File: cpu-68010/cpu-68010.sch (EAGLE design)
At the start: 5 parts, among them X1 FABC96R

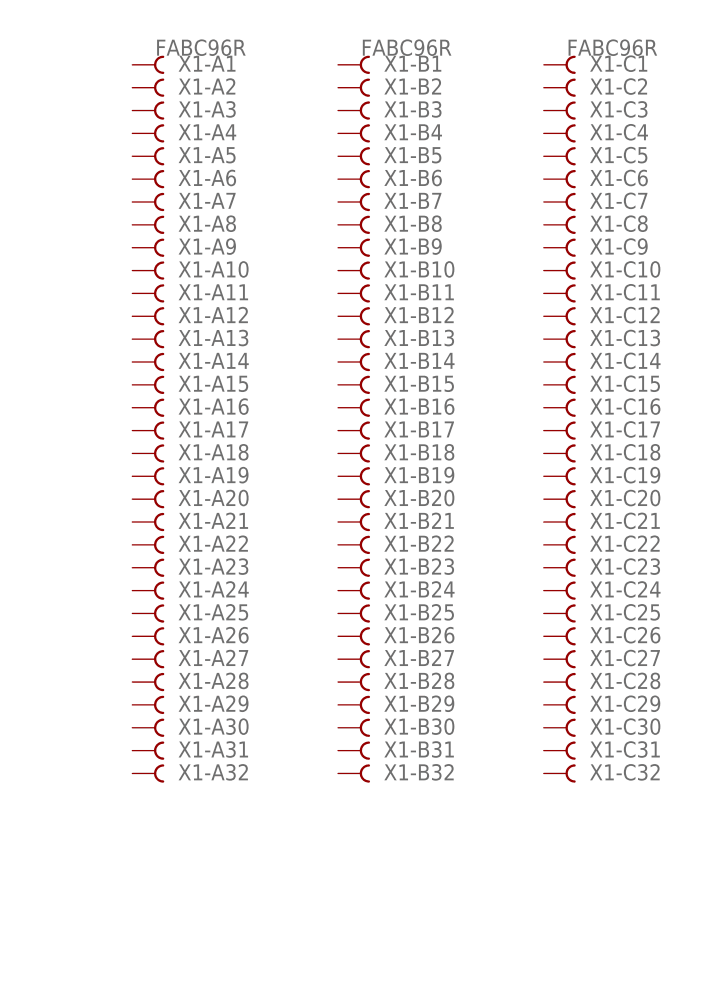
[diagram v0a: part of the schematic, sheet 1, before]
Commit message: added bus pinout description, basic connections for bus
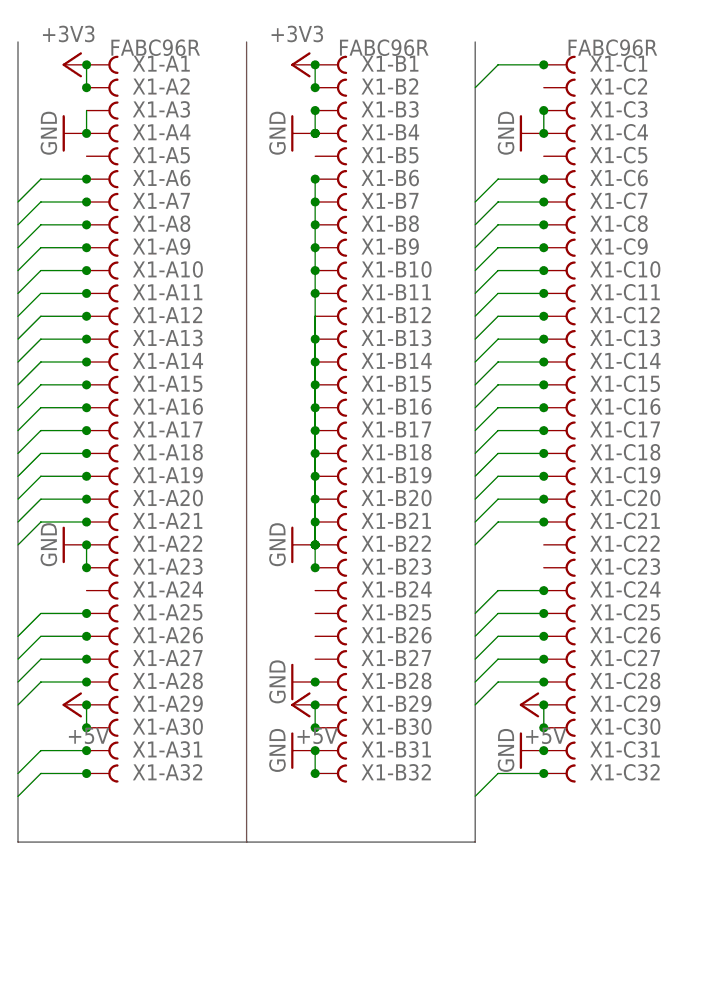
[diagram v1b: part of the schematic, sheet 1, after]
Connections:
- new net !BUS_ACK: X1-A28.B
- new net !BUS_IRQ: X1-A31.B
- new net !BUS_IRQACK: X1-A32.B
- new net !BUS_RESET: X1-C1.B
- new net !BUS_START: X1-C28.B
- new net +3V3: X1-A1.B, X1-A2.B, X1-B1.B, X1-B2.B
- new net BUS_AD0: X1-C6.B
- new net BUS_AD1: X1-A6.B
- new net BUS_AD10: X1-C11.B
- new net BUS_AD11: X1-A11.B
- new net BUS_AD12: X1-C12.B
- new net BUS_AD13: X1-A12.B
- new net BUS_AD14: X1-C13.B
- new net BUS_AD15: X1-A13.B
- new net BUS_AD16: X1-C14.B
- new net BUS_AD17: X1-A14.B
- new net BUS_AD18: X1-C15.B
- new net BUS_AD19: X1-A15.B
- new net BUS_AD2: X1-C7.B
- new net BUS_AD20: X1-C16.B
- new net BUS_AD21: X1-A16.B
- new net BUS_AD22: X1-C17.B
- new net BUS_AD23: X1-A17.B
- new net BUS_AD24: X1-C18.B
- new net BUS_AD25: X1-A18.B
- new net BUS_AD26: X1-C19.B
- new net BUS_AD27: X1-A19.B
- new net BUS_AD28: X1-C20.B
- new net BUS_AD29: X1-A20.B
- new net BUS_AD3: X1-A7.B
- new net BUS_AD30: X1-C21.B
- new net BUS_AD31: X1-A21.B
- new net BUS_AD4: X1-C8.B
- new net BUS_AD5: X1-A8.B
- new net BUS_AD6: X1-C9.B
- new net BUS_AD7: X1-A9.B
- new net BUS_AD8: X1-C10.B
- new net BUS_AD9: X1-A10.B
- new net BUS_CLK: X1-C32.B
- new net BUS_CONFIG: X1-A25.B
- new net BUS_CS0: X1-C26.B
- new net BUS_CS1: X1-A26.B
- new net BUS_CS2: X1-C27.B
- new net BUS_CS3: X1-A27.B
- new net BUS_MODE0: X1-C24.B
- new net BUS_MODE1: X1-C25.B
- net +5V: now also X1-A29.B, X1-A30.B, X1-B29.B, X1-B30.B, X1-C29.B, X1-C30.B
- net GND: now also X1-A22.B, X1-A23.B, X1-A3.B, X1-A4.B, X1-B10.B, X1-B11.B, X1-B12.B, X1-B13.B, X1-B14.B, X1-B15.B, X1-B16.B, X1-B17.B, X1-B18.B, X1-B19.B, X1-B20.B, X1-B21.B, X1-B22.B, X1-B23.B, X1-B28.B, X1-B3.B, X1-B31.B, X1-B32.B, X1-B4.B, X1-B6.B, X1-B7.B, X1-B8.B, X1-B9.B, X1-C3.B, X1-C31.B, X1-C4.B
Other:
- moved on the sheet: X1-A1, X1-A10, X1-A11, X1-A12, X1-A13, X1-A14, X1-A15, X1-A16, X1-A17, X1-A18, X1-A19, X1-A2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

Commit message: added psram to 68010 board
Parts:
- added C2, C5: 100nF, rcl:C-EUC0805
- added C4: 47µF, rcl:CPOL-EUCT6032
- added IC2: (no value), 68komputer:IS66WV51216EBLLTSOP-44
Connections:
- new net !RAM_CS: IC2.!CS1
- new net !RAM_LB: IC2.!LB
- new net !RAM_OE: IC2.!OE
- new net !RAM_UB: IC2.!UB
- new net !RAM_WE: IC2.!WE
- new net A1: IC2.A0
- new net A10: IC2.A9
- new net A11: IC2.A10
- new net A12: IC2.A11
- new net A13: IC2.A12
- new net A14: IC2.A13
- new net A15: IC2.A14
- new net A16: IC2.A15
- new net A17: IC2.A16
- new net A18: IC2.A17
- new net A19: IC2.A18
- new net A2: IC2.A1
- new net A3: IC2.A2
- new net A4: IC2.A3
- new net A5: IC2.A4
- new net A6: IC2.A5
- new net A7: IC2.A6
- new net A8: IC2.A7
- new net A9: IC2.A8
- new net D0: IC2.D0
- new net D1: IC2.D1
- new net D10: IC2.D10
- new net D11: IC2.D11
- new net D12: IC2.D12
- new net D13: IC2.D13
- new net D14: IC2.D14
- new net D15: IC2.D15
- new net D2: IC2.D2
- new net D3: IC2.D3
- new net D4: IC2.D4
- new net D5: IC2.D5
- new net D6: IC2.D6
- new net D7: IC2.D7
- new net D8: IC2.D8
- new net D9: IC2.D9
- net +3V3: now also C2.1, C4.+, C5.1, IC2.VDD
- net GND: now also C2.2, C4.-, C5.2, IC2.GND

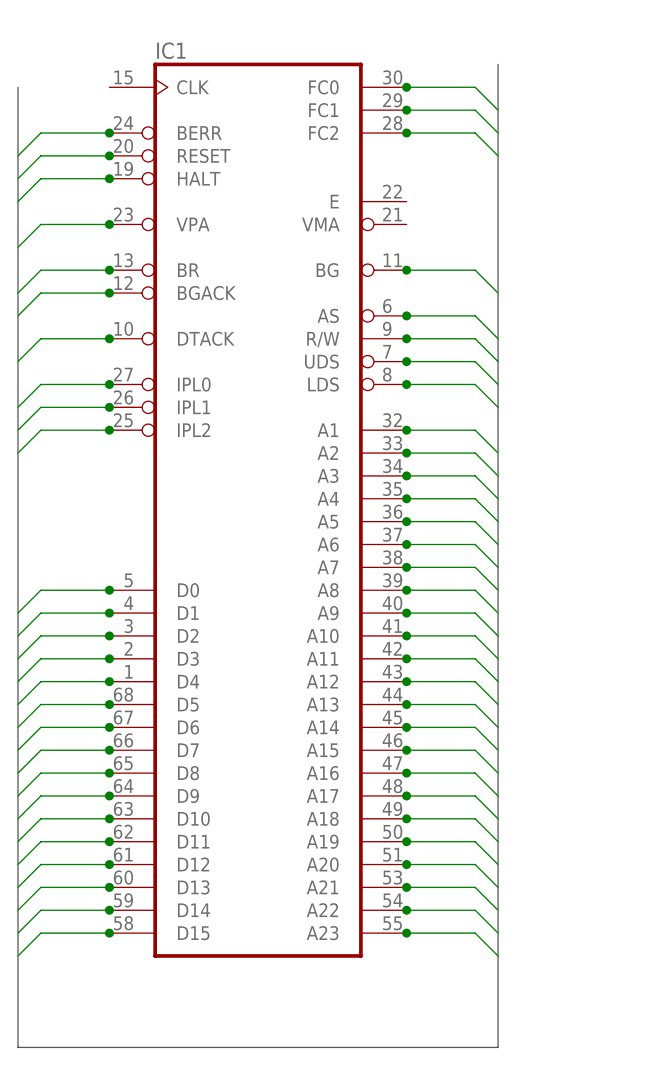
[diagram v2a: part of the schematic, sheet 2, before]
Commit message: cleaned up kerjigger somewhat
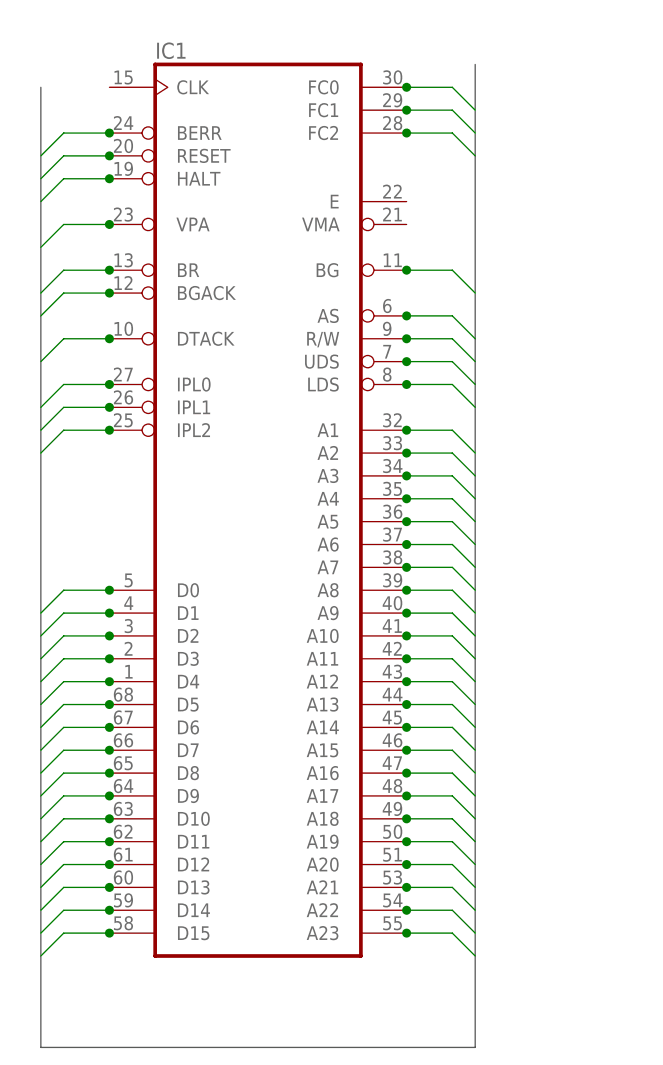
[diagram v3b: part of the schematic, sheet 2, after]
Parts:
- added C10, C12, C13, C7, C9: 100nF, rcl:C-EUC0805
- added C11, C8: 47µF, rcl:CPOL-EUCT6032
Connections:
- net +3V3: now also C10.1, C11.+, C12.1
- net +5V: now also C13.1, C7.1, C8.+, C9.1
- net GND: now also C10.2, C11.-, C12.2, C13.2, C7.2, C8.-, C9.2

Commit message: added address decoding, interrupt handling, external bus interface
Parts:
- added C14, C16, C17, C19, C20, C21, C23, C24, C25, C26: 100nF, rcl:C-EUC0805
- added C15, C18, C22: 47µF, rcl:CPOL-EUCT6032
- added C27, C28, C29, C30: 10µF, rcl:CPOL-EUE1.8-4
- added IC10, IC11: 74HC30D, 74xx-eu:74HC30D
- added IC12: 74HC85D, 74xx-eu:74HC85D
- added IC13: MAX232, maxim:MAX232
- added IC3, IC4: (no value), 68komputer:SST39SF0X0PDIP-32
- added IC5: (no value), 68komputer:DS1244EDIP-28
- added IC6: 74HC00D, 74xx-eu:74HC00D
- added IC7: 74HCT154DW, 74xx-eu:74HCT154DW
- added IC8: 74HC04D, 74xx-eu:74HC04D
- added IC9: 74HC148D, 74xx-eu:74HC148D
- added QG1: (no value), crystal:XO-8
- added R1: 10k, rcl:R-EU_R2012
- added X2: (no value), con-subd:F09HP
- C10: value 100nF -> 47µF; device rcl:C-EUC0805 -> rcl:CPOL-EUCT6032; MOUSER 710-885012207072 -> 581-TAJD476M016RNJV
- C11: value 47µF -> 100nF; device rcl:CPOL-EUCT6032 -> rcl:C-EUC0805; MOUSER 581-TAJD476M016RNJV -> 710-885012207072
- IC1: device micro-mc68000:MC68000FN-SOC -> 68komputer:MC68000FN-SOC
- IC2: device 68komputer:IS66WV51216EBLLTSOP-44 -> 68komputer:MC68901FN-SOC
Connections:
- removed net !68K_AS: IC1G$1.AS
- removed net !68K_BERR: IC1G$1.BERR
- removed net !68K_BG: IC1G$1.BG
- removed net !68K_BGACK: IC1G$1.BGACK
- removed net !68K_BR: IC1G$1.BR
- removed net !68K_DTACK: IC1G$1.DTACK
- removed net !68K_HALT: IC1G$1.HALT
- removed net !68K_IPL0: IC1G$1.IPL0
- removed net !68K_IPL1: IC1G$1.IPL1
- removed net !68K_IPL2: IC1G$1.IPL2
- removed net !68K_LDS: IC1G$1.LDS
- removed net !68K_RESET: IC1G$1.RESET
- removed net !68K_UDS: IC1G$1.UDS
- removed net !68K_VPA: IC1G$1.VPA
- removed net !BUS_ACK: X1-A28.B
- removed net !BUS_IRQ: X1-A31.B
- removed net !BUS_IRQACK: X1-A32.B
- removed net !BUS_RESET: X1-C1.B
- removed net !BUS_START: X1-C28.B
- removed net !RAM_CS: IC2.!CS1
- removed net !RAM_LB: IC2.!LB
- removed net !RAM_OE: IC2.!OE
- removed net !RAM_UB: IC2.!UB
- removed net !RAM_WE: IC2.!WE
- removed net +3V3: C10.1, C11.+, C12.1, C2.1, C4.+, C5.1, IC2.VDD, X1-A1.B, X1-A2.B, X1-B1.B, X1-B2.B
- removed net 68K_A1: IC1G$1.A1
- removed net 68K_A10: IC1G$1.A10
- removed net 68K_A11: IC1G$1.A11
- removed net 68K_A12: IC1G$1.A12
- removed net 68K_A13: IC1G$1.A13
- removed net 68K_A14: IC1G$1.A14
- removed net 68K_A15: IC1G$1.A15
- removed net 68K_A16: IC1G$1.A16
- removed net 68K_A17: IC1G$1.A17
- removed net 68K_A18: IC1G$1.A18
- removed net 68K_A19: IC1G$1.A19
- removed net 68K_A2: IC1G$1.A2
- removed net 68K_A20: IC1G$1.A20
- removed net 68K_A21: IC1G$1.A21
- removed net 68K_A22: IC1G$1.A22
- removed net 68K_A23: IC1G$1.A23
- removed net 68K_A3: IC1G$1.A3
- removed net 68K_A4: IC1G$1.A4
- removed net 68K_A5: IC1G$1.A5
- removed net 68K_A6: IC1G$1.A6
- removed net 68K_A7: IC1G$1.A7
- removed net 68K_A8: IC1G$1.A8
- removed net 68K_A9: IC1G$1.A9
- removed net 68K_D0: IC1G$1.D0
- removed net 68K_D1: IC1G$1.D1
- removed net 68K_D10: IC1G$1.D10
- removed net 68K_D11: IC1G$1.D11
- removed net 68K_D12: IC1G$1.D12
- removed net 68K_D13: IC1G$1.D13
- removed net 68K_D14: IC1G$1.D14
- removed net 68K_D15: IC1G$1.D15
- removed net 68K_D2: IC1G$1.D2
- removed net 68K_D3: IC1G$1.D3
- removed net 68K_D4: IC1G$1.D4
- removed net 68K_D5: IC1G$1.D5
- removed net 68K_D6: IC1G$1.D6
- removed net 68K_D7: IC1G$1.D7
- removed net 68K_D8: IC1G$1.D8
- removed net 68K_D9: IC1G$1.D9
- removed net 68K_FC0: IC1G$1.FC0
- removed net 68K_FC1: IC1G$1.FC1
- removed net 68K_FC2: IC1G$1.FC2
- removed net 68K_R!W!: IC1G$1.R/W
- removed net BUS_AD0: X1-C6.B
- removed net BUS_AD1: X1-A6.B
- removed net BUS_AD10: X1-C11.B
- removed net BUS_AD11: X1-A11.B
- removed net BUS_AD12: X1-C12.B
- removed net BUS_AD13: X1-A12.B
- removed net BUS_AD14: X1-C13.B
- removed net BUS_AD15: X1-A13.B
- removed net BUS_AD16: X1-C14.B
- removed net BUS_AD17: X1-A14.B
- removed net BUS_AD18: X1-C15.B
- removed net BUS_AD19: X1-A15.B
- removed net BUS_AD2: X1-C7.B
- removed net BUS_AD20: X1-C16.B
- removed net BUS_AD21: X1-A16.B
- removed net BUS_AD22: X1-C17.B
- removed net BUS_AD23: X1-A17.B
- removed net BUS_AD24: X1-C18.B
- removed net BUS_AD25: X1-A18.B
- removed net BUS_AD26: X1-C19.B
- removed net BUS_AD27: X1-A19.B
- removed net BUS_AD28: X1-C20.B
- removed net BUS_AD29: X1-A20.B
- removed net BUS_AD3: X1-A7.B
- removed net BUS_AD30: X1-C21.B
- removed net BUS_AD31: X1-A21.B
- removed net BUS_AD4: X1-C8.B
- removed net BUS_AD5: X1-A8.B
- removed net BUS_AD6: X1-C9.B
- removed net BUS_AD7: X1-A9.B
- removed net BUS_AD8: X1-C10.B
- removed net BUS_AD9: X1-A10.B
- removed net BUS_CLK: X1-C32.B
- removed net BUS_CONFIG: X1-A25.B
- removed net BUS_CS0: X1-C26.B
- removed net BUS_CS1: X1-A26.B
- removed net BUS_CS2: X1-C27.B
- removed net BUS_CS3: X1-A27.B
- removed net BUS_MODE0: X1-C24.B
- removed net BUS_MODE1: X1-C25.B
- new net !68901_CS: IC2G$1.CS, IC6A.O
- new net !68901_DTACK: IC10A.I0, IC2G$1.DTACK, R1.1
- new net !68901_IACK: IC2G$1.IACK
- new net !68901_IRQ: IC2G$1.IRQ, IC9A.6
- new net !A19: IC6A.I1, IC8C.O
- new net !AS: IC1G$1.AS, X1-B21.B
- new net !BERR: IC1G$1.BERR, X1-B9.B
- new net !BG: IC1G$1.BG, X1-B14.B
- new net !BGACK: IC1G$1.BGACK, X1-B15.B
- new net !BR: IC1G$1.BR, X1-B13.B
- new net !DTACK: IC1G$1.DTACK, IC8D.O
- new net !EXT_DTACK: IC10A.I1, X1-B28.B
- new net !EXT_IRQ: IC9A.4, X1-B17.B
- new net !HALT: IC1G$1.HALT, X1-B11.B
- new net !IPL0: IC1G$1.IPL0, IC9A.A0
- new net !IPL1: IC1G$1.IPL1, IC9A.A1
- new net !IPL2: IC1G$1.IPL2, IC9A.A2
- new net !LDS: IC1G$1.LDS, IC2G$1.DS, X1-B24.B
- new net !NMI: IC9A.7
- new net !OE: IC3.!OE, IC4.!OE, IC5.!OE, IC8A.O
- new net !REGION0: IC10A.I2, IC3.!CS, IC4.!CS, IC7A.0
- new net !REGION1: IC10A.I3, IC7A.1
- new net !REGION10: IC7A.10
- new net !REGION11: IC7A.11
- new net !REGION12: IC7A.12
- new net !REGION13: IC7A.13
- new net !REGION14: IC7A.14
- new net !REGION15: IC7A.15, IC8B.I
- new net !REGION2: IC7A.2
- new net !REGION3: IC7A.3
- new net !REGION4: IC7A.4
- new net !REGION5: IC7A.5
- new net !REGION6: IC7A.6
- new net !REGION7: IC7A.7
- new net !REGION8: IC7A.8
- new net !REGION9: IC7A.9
- new net !RESET: IC1G$1.RESET, IC2G$1.RESET, X1-B10.B
- new net !ROM_WE: IC3.!WE, IC4.!WE
- new net !RTC_CS: IC10A.I4, IC5.!CS, IC6B.O
- new net !UDS: IC1G$1.UDS, X1-B23.B
- new net !VMA: IC1G$1.VMA
- new net !VPA: IC11A.O, IC1G$1.VPA, X1-B12.B
- new net /AS: IC7A.G1, IC7A.G2
- new net A20: IC1G$1.A20, IC7A.A, X1-A21.B
- new net A21: IC1G$1.A21, IC7A.B, X1-A22.B
- new net A22: IC1G$1.A22, IC7A.C, X1-A23.B
- new net A23: IC1G$1.A23, IC7A.D, X1-A24.B
- new net CLK: IC1G$1.CLK, IC2G$1.CLK, IC2G$1.XTAL1, QG1.OUT, X1-B26.B
- new net DTACK: IC10A.O, IC8D.I
- new net E: IC1G$1.E
- new net FC0: IC11A.I0, IC1G$1.FC0, X1-B6.B
- new net FC1: IC11A.I1, IC1G$1.FC1, X1-B7.B
- new net FC2: IC11A.I2, IC1G$1.FC2, X1-B8.B
- new net GPIO0: IC2G$1.I0
- new net GPIO1: IC2G$1.I1
- new net GPIO2: IC2G$1.I2
- new net GPIO3: IC2G$1.I3
- new net GPIO4: IC2G$1.I4
- new net GPIO5: IC2G$1.I5
- new net GPIO6: IC2G$1.I6
- new net GPIO7: IC2G$1.I7
- new net N$1: C27.+, IC13G$1.V+
- new net N$2: C28.-, IC13G$1.V-
- new net N$3: C29.+, IC13G$1.C1+
- new net N$4: C30.+, IC13G$1.C2+
- new net N$5: C29.-, IC13G$1.C1-
- new net N$6: C30.-, IC13G$1.C2-
- new net R!W!: IC1G$1.R/W, IC2G$1.R/!W, IC5.!WE, IC8A.I, X1-B22.B
- new net REGION15: IC6A.I0, IC6B.I0, IC8B.O
- new net RS232_RX: IC13G$1.T1OUT, X2.2
- new net RS232_TX: IC13G$1.R1IN, X2.3
- new net UART_CLK: IC2G$1.RC, IC2G$1.TC
- new net UART_RX: IC13G$1.R1OUT, IC2G$1.SI
- new net UART_TX: IC13G$1.T1IN, IC2G$1.SO
- net +5V: now also C10.+, C11.1, C12.1, C14.1, C15.+, C16.1, C17.1, C18.+, C19.1, C2.1, C20.1, C21.1, C22.+, C23.1, C24.1, C25.1, C26.1, C27.-, C4.+, C5.1, IC10A.I5, IC10A.I6, IC10A.I7, IC10P.VCC, IC11A.I7, IC11P.VCC, IC12P.VCC, IC13P.VCC, IC2P.VCC, IC3.VCC, IC4.VCC, IC5.VCC, IC6P.VCC, IC7P.VCC, IC8P.VCC, IC9A.1, IC9A.2, IC9A.3, IC9A.5, IC9P.VCC, QG1.VCC, R1.2, X1-B1.B, X1-B2.B, X1-B3.B; no longer X1-A29.B, X1-A30.B, X1-B29.B, X1-B30.B, X1-C29.B, X1-C30.B
- net A1: now also IC1G$1.A1, IC2G$1.A1, IC3.A0, IC4.A0, IC5.A0, X1-A2.B; no longer IC2.A0
- net A10: now also IC1G$1.A10, IC3.A9, IC4.A9, IC5.A9, X1-A11.B; no longer IC2.A9
- net A11: now also IC1G$1.A11, IC3.A10, IC4.A10, IC5.A10, X1-A12.B; no longer IC2.A10
- net A12: now also IC1G$1.A12, IC3.A11, IC4.A11, IC5.A11, X1-A13.B; no longer IC2.A11
- net A13: now also IC1G$1.A13, IC3.A12, IC4.A12, IC5.A12, X1-A14.B; no longer IC2.A12
- net A14: now also IC1G$1.A14, IC3.A13, IC4.A13, IC5.A13, X1-A15.B; no longer IC2.A13
- net A15: now also IC1G$1.A15, IC3.A14, IC4.A14, IC5.A14, X1-A16.B; no longer IC2.A14
- net A16: now also IC11A.I3, IC1G$1.A16, IC3.A15, IC4.A15, X1-A17.B; no longer IC2.A15
- net A17: now also IC11A.I4, IC1G$1.A17, IC3.A16, IC4.A16, X1-A18.B; no longer IC2.A16
- net A18: now also IC11A.I5, IC1G$1.A18, IC3.A17, IC4.A17, X1-A19.B; no longer IC2.A17
- net A19: now also IC11A.I6, IC1G$1.A19, IC3.A18, IC4.A18, IC6B.I1, IC8C.I, X1-A20.B; no longer IC2.A18
- net A2: now also IC1G$1.A2, IC2G$1.A2, IC3.A1, IC4.A1, IC5.A1, X1-A3.B; no longer IC2.A1
- net A3: now also IC1G$1.A3, IC2G$1.A3, IC3.A2, IC4.A2, IC5.A2, X1-A4.B; no longer IC2.A2
- net A4: now also IC1G$1.A4, IC2G$1.A4, IC3.A3, IC4.A3, IC5.A3, X1-A5.B; no longer IC2.A3
- net A5: now also IC1G$1.A5, IC2G$1.A5, IC3.A4, IC4.A4, IC5.A4, X1-A6.B; no longer IC2.A4
- net A6: now also IC1G$1.A6, IC3.A5, IC4.A5, IC5.A5, X1-A7.B; no longer IC2.A5
- net A7: now also IC1G$1.A7, IC3.A6, IC4.A6, IC5.A6, X1-A8.B; no longer IC2.A6
- net A8: now also IC1G$1.A8, IC3.A7, IC4.A7, IC5.A7, X1-A9.B; no longer IC2.A7
- net A9: now also IC1G$1.A9, IC3.A8, IC4.A8, IC5.A8, X1-A10.B; no longer IC2.A8
- net D0: now also IC1G$1.D0, IC2G$1.D0, IC4.DQ0, IC5.DQ0, X1-C1.B; no longer IC2.D0
- net D1: now also IC1G$1.D1, IC2G$1.D1, IC4.DQ1, IC5.DQ1, X1-C2.B; no longer IC2.D1
- net D10: now also IC1G$1.D10, IC3.DQ2, X1-C11.B; no longer IC2.D10
- net D11: now also IC1G$1.D11, IC3.DQ3, X1-C12.B; no longer IC2.D11
- net D12: now also IC1G$1.D12, IC3.DQ4, X1-C13.B; no longer IC2.D12
- net D13: now also IC1G$1.D13, IC3.DQ5, X1-C14.B; no longer IC2.D13
- net D14: now also IC1G$1.D14, IC3.DQ6, X1-C15.B; no longer IC2.D14
- net D15: now also IC1G$1.D15, IC3.DQ7, X1-C16.B; no longer IC2.D15
- net D2: now also IC1G$1.D2, IC2G$1.D2, IC4.DQ2, IC5.DQ2, X1-C3.B; no longer IC2.D2
- net D3: now also IC1G$1.D3, IC2G$1.D3, IC4.DQ3, IC5.DQ3, X1-C4.B; no longer IC2.D3
- net D4: now also IC1G$1.D4, IC2G$1.D4, IC4.DQ4, IC5.DQ4, X1-C5.B; no longer IC2.D4
- net D5: now also IC1G$1.D5, IC2G$1.D5, IC4.DQ5, IC5.DQ5, X1-C6.B; no longer IC2.D5
- net D6: now also IC1G$1.D6, IC2G$1.D6, IC4.DQ6, IC5.DQ6, X1-C7.B; no longer IC2.D6
- net D7: now also IC1G$1.D7, IC2G$1.D7, IC4.DQ7, IC5.DQ7, X1-C8.B; no longer IC2.D7
- net D8: now also IC1G$1.D8, IC3.DQ0, X1-C9.B; no longer IC2.D8
- net D9: now also IC1G$1.D9, IC3.DQ1, X1-C10.B; no longer IC2.D9
- net GND: now also C10.-, C11.2, C14.2, C15.-, C16.2, C17.2, C18.-, C19.2, C20.2, C21.2, C22.-, C23.2, C24.2, C25.2, C26.2, C28.+, IC10P.GND, IC11P.GND, IC12P.GND, IC13P.GND, IC2G$1.IEI, IC2P.GND, IC3.GND, IC4.GND, IC5.GND, IC6P.GND, IC7P.GND, IC8P.GND, IC9A.0, IC9A.EI, IC9P.GND, QG1.GND, X1-A25.B, X1-A26.B, X1-A27.B, X1-A28.B, X1-A29.B, X1-A30.B, X1-A31.B, X1-A32.B, X1-B25.B, X1-B27.B, X1-B30.B, X2.5, X2.G1, X2.G2; no longer C10.2, C11.-, IC2.GND, X1-A22.B, X1-A23.B, X1-A3.B, X1-A4.B, X1-B10.B, X1-B11.B, X1-B12.B, X1-B13.B, X1-B14.B, X1-B15.B, X1-B16.B, X1-B17.B, X1-B18.B, X1-B19.B, X1-B20.B, X1-B21.B, X1-B22.B, X1-B23.B, X1-B28.B, X1-B3.B, X1-B4.B, X1-B6.B, X1-B7.B, X1-B8.B, X1-B9.B, X1-C3.B, X1-C31.B, X1-C4.B
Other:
- note added: "All interrupts will be autovectored"
- note added: "Generated Signals: /MCS: ~(~A[19] & ~REGION[15]) /RCS: ~(A[19] & ~REGION[15])"
- note added: "Generated Signals: OE: ~R/!W"
- note added: "High ROM"
- note added: "IC1 is CPU: can be 68000 or 68010"
- note added: "IC3/IC4 can be one of SST39SF0[1,2,4]0"
- note added: "Low ROM"
- note added: "Memory Map $000000 - $0FFFFF: ROM $100000 - $1FFFFF: RAM $F00000 - $FFFFFF: On-board peripherals"
- note added: "Memory Map $F00000 - $F7FFFF: 68901 $F80000 - $FFFFFF: RTC"
- note added: "RAM is decoded for $100000-$1FFFFF No waitstates are inserted"
- note added: "ROM is decoded for $000000-$0FFFFF (1MB) No waitstates are inserted"
